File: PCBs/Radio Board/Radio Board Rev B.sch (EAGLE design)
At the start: 10 parts

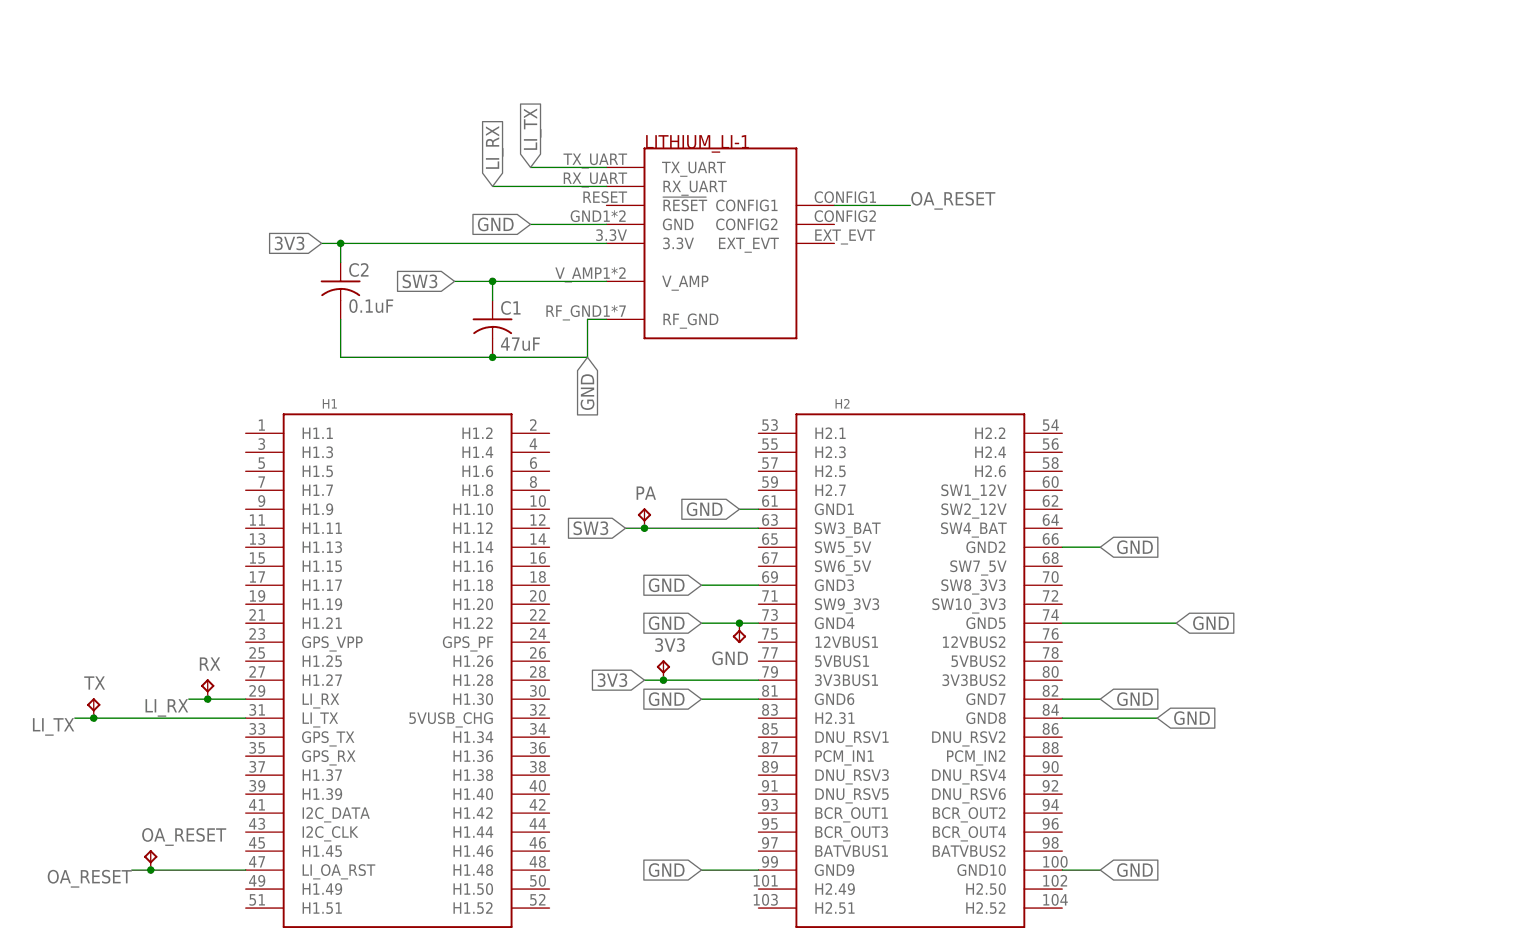
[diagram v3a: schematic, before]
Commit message: Add Molex connector and connector bypass to radio board
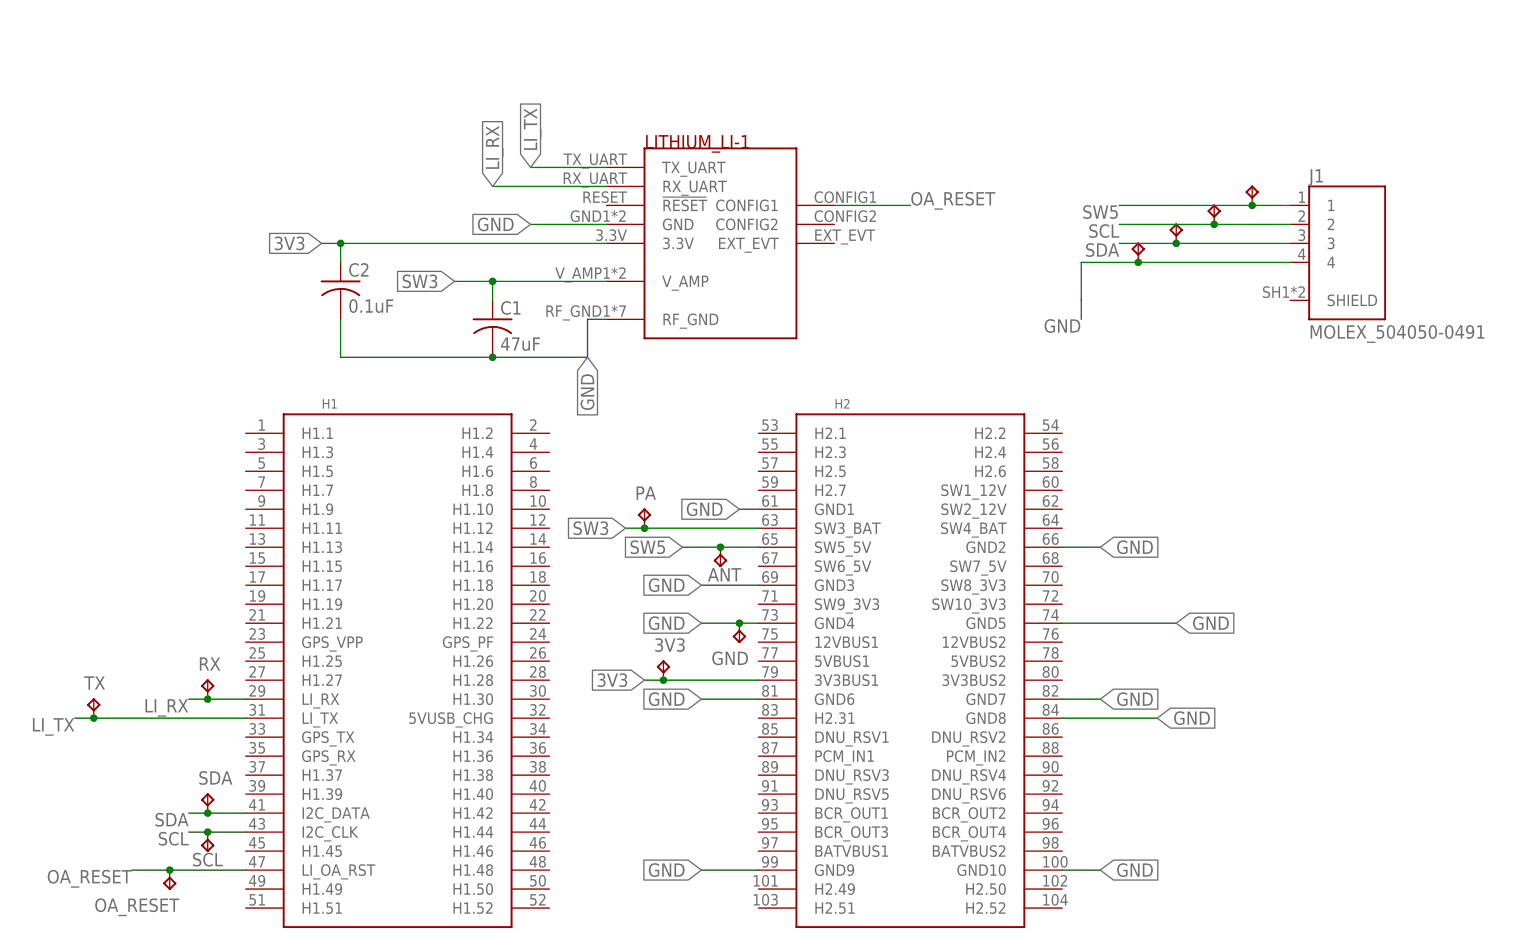
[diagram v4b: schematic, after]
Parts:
- added ANT, J1_1, J1_2, J1_3, J1_4, SCL, SDA: TPTP10SQ, testpad:TPTP10SQ
- added J1: MOLEX_504050-0491, Molex 504050-0491:MOLEX_504050-0491
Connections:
- new net SCL: J1.2, J1_2.TP, SCL.TP, U$1.I2C_CLK
- new net SDA: J1.3, J1_3.TP, SDA.TP, U$1.I2C_DATA
- new net SW5: ANT.TP, J1.1, J1_1.TP, U$1.SW5_5V
- net GND: now also J1.4, J1_4.TP
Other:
- moved on the sheet: OA_RESET
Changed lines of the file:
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@@
 <part name="PA" library="testpad" library_urn="urn:adsk.eagle:library:385" deviceset="TP" device="TP10SQ" package3d_urn="urn:adsk.eagle:package:27962/1"/>
 <part name="GND" library="testpad" library_urn="urn:adsk.eagle:library:385" deviceset="TP" device="TP10SQ" package3d_urn="urn:adsk.eagle:package:27962/1"/>
+<part name="J1" library="Molex 504050-0491" deviceset="MOLEX_504050-0491" device=""/>
+<part name="SDA" library="testpad" library_urn="urn:adsk.eagle:library:385" deviceset="TP" device="TP10SQ" package3d_urn="urn:adsk.eagle:package:27962/1"/>
+<part name="SCL" library="testpad" library_urn="urn:adsk.eagle:library:385" deviceset="TP" device="TP10SQ" package3d_urn="urn:adsk.eagle:package:27962/1"/>
+<part name="ANT" library="testpad" library_urn="urn:adsk.eagle:library:385" deviceset="TP" device="TP10SQ" package3d_urn="urn:adsk.eagle:package:27962/1"/>
+<part name="J1_1" library="testpad" library_urn="urn:adsk.eagle:library:385" deviceset="TP" device="TP10SQ" package3d_urn="urn:adsk.eagle:package:27962/1"/>
+<part name="J1_2" library="testpad" library_urn="urn:adsk.eagle:library:385" deviceset="TP" device="TP10SQ" package3d_urn="urn:adsk.eagle:package:27962/1"/>
+<part name="J1_3" library="testpad" library_urn="urn:adsk.eagle:library:385" deviceset="TP" device="TP10SQ" package3d_urn="urn:adsk.eagle:package:27962/1"/>
+<part name="J1_4" library="testpad" library_urn="urn:adsk.eagle:library:385" deviceset="TP" device="TP10SQ" package3d_urn="urn:adsk.eagle:package:27962/1"/>
 </parts>
 <sheets>
@@
 <instance part="RX" gate="G$1" x="17.78" y="33.02"/>
 <instance part="TX" gate="G$1" x="2.54" y="30.48"/>
-<instance part="OA_RESET" gate="G$1" x="10.16" y="10.16"/>
+<instance part="OA_RESET" gate="G$1" x="12.7" y="5.08" rot="R180"/>
 <instance part="PA" gate="G$1" x="76.2" y="55.88"/>
 <instance part="GND" gate="G$1" x="88.9" y="38.1" rot="R180"/>
+<instance part="J1" gate="G$1" x="170.18" y="91.44"/>
+<instance part="SDA" gate="G$1" x="17.78" y="17.78"/>
+<instance part="SCL" gate="G$1" x="17.78" y="10.16" smashed="yes" rot="R180">
+<attribute name="NAME" x="19.812" y="9.906" size="1.778" layer="95" rot="R180"/>
+<attribute name="TP_SIGNAL_NAME" x="16.51" y="11.43" size="1.778" layer="97" rot="R180"/>
+</instance>
+<instance part="ANT" gate="G$1" x="86.36" y="48.26" smashed="yes" rot="R180">
+<attribute name="NAME" x="89.154" y="48.006" size="1.778" layer="95" rot="R180"/>
+<attribute name="TP_SIGNAL_NAME" x="85.09" y="49.53" size="1.778" layer="97" rot="R180"/>
+</instance>
+<instance part="J1_1" gate="G$1" x="157.48" y="99.06" smashed="yes">
+<attribute name="TP_SIGNAL_NAME" x="158.75" y="97.79" size="1.778" layer="97"/>
+</instance>
+<instance part="J1_2" gate="G$1" x="152.4" y="96.52" smashed="yes">
+<attribute name="TP_SIGNAL_NAME" x="153.67" y="95.25" size="1.778" layer="97"/>
+</instance>
+<instance part="J1_3" gate="G$1" x="147.32" y="93.98" smashed="yes">
+<attribute name="TP_SIGNAL_NAME" x="148.59" y="92.71" size="1.778" layer="97"/>
+</instance>
+<instance part="J1_4" gate="G$1" x="142.24" y="91.44" smashed="yes">
+<attribute name="TP_SIGNAL_NAME" x="143.51" y="90.17" size="1.778" layer="97"/>
+</instance>
 </instances>
 <busses>
@@
 <pinref part="LI-1" gate="G$1" pin="RF_GND"/>
 </segment>
+<segment>
+<wire x1="134.62" y1="83.82" x2="134.62" y2="81.28" width="0.1524" layer="91"/>
+<label x="134.62" y="81.28" size="1.778" layer="95" rot="R180"/>
+<pinref part="J1" gate="G$1" pin="4"/>
+<wire x1="162.56" y1="88.9" x2="142.24" y2="88.9" width="0.1524" layer="91"/>
+<wire x1="142.24" y1="88.9" x2="134.62" y2="88.9" width="0.1524" layer="91"/>
+<wire x1="134.62" y1="88.9" x2="134.62" y2="83.82" width="0.1524" layer="91"/>
+<pinref part="J1_4" gate="G$1" pin="TP"/>
+<junction x="142.24" y="88.9"/>
+</segment>
 </net>
 <net name="SW3" class="0">
@@
 </segment>
 <segment>
-<wire x1="22.86" y1="7.62" x2="10.16" y2="7.62" width="0.1524" layer="91"/>
+<wire x1="22.86" y1="7.62" x2="12.7" y2="7.62" width="0.1524" layer="91"/>
 <label x="7.62" y="7.62" size="1.778" layer="95" rot="R180"/>
 <pinref part="U$1" gate="A" pin="LI_OA_RST"/>
 <pinref part="OA_RESET" gate="G$1" pin="TP"/>
-<wire x1="10.16" y1="7.62" x2="7.62" y2="7.62" width="0.1524" layer="91"/>
-<junction x="10.16" y="7.62"/>
+<wire x1="12.7" y1="7.62" x2="7.62" y2="7.62" width="0.1524" layer="91"/>
+<junction x="12.7" y="7.62"/>
 </segment>
 </net>
@@
 </segment>
 </net>
+<net name="SW5" class="0">
+<segment>
+<pinref part="J1" gate="G$1" pin="1"/>
+<wire x1="162.56" y1="96.52" x2="157.48" y2="96.52" width="0.1524" layer="91"/>
+<label x="139.7" y="96.52" size="1.778" layer="95" rot="R180"/>
+<pinref part="J1_1" gate="G$1" pin="TP"/>
+<wire x1="157.48" y1="96.52" x2="139.7" y2="96.52" width="0.1524" layer="91"/>
+<junction x="157.48" y="96.52"/>
+</segment>
+<segment>
+<pinref part="U$1" gate="A" pin="SW5_5V"/>
+<wire x1="91.44" y1="50.8" x2="86.36" y2="50.8" width="0.1524" layer="91"/>
+<label x="81.28" y="50.8" size="1.778" layer="95" rot="R180" xref="yes"/>
+<pinref part="ANT" gate="G$1" pin="TP"/>
+<wire x1="86.36" y1="50.8" x2="81.28" y2="50.8" width="0.1524" layer="91"/>
+<junction x="86.36" y="50.8"/>
+</segment>
+</net>
+<net name="SCL" class="0">
+<segment>
+<pinref part="J1" gate="G$1" pin="2"/>
+<wire x1="162.56" y1="93.98" x2="152.4" y2="93.98" width="0.1524" layer="91"/>
+<label x="139.7" y="93.98" size="1.778" layer="95" rot="R180"/>
+<pinref part="J1_2" gate="G$1" pin="TP"/>
+<wire x1="152.4" y1="93.98" x2="139.7" y2="93.98" width="0.1524" layer="91"/>
+<junction x="152.4" y="93.98"/>
+</segment>
+<segment>
+<pinref part="U$1" gate="A" pin="I2C_CLK"/>
+<wire x1="22.86" y1="12.7" x2="17.78" y2="12.7" width="0.1524" layer="91"/>
+<label x="15.24" y="12.7" size="1.778" layer="95" rot="R180"/>
+<pinref part="SCL" gate="G$1" pin="TP"/>
+<wire x1="17.78" y1="12.7" x2="15.24" y2="12.7" width="0.1524" layer="91"/>
+<junction x="17.78" y="12.7"/>
+</segment>
+</net>
+<net name="SDA" class="0">
+<segment>
+<pinref part="J1" gate="G$1" pin="3"/>
+<wire x1="162.56" y1="91.44" x2="147.32" y2="91.44" width="0.1524" layer="91"/>
+<label x="139.7" y="91.44" size="1.778" layer="95" rot="R180"/>
+<pinref part="J1_3" gate="G$1" pin="TP"/>
+<wire x1="147.32" y1="91.44" x2="139.7" y2="91.44" width="0.1524" layer="91"/>
+<junction x="147.32" y="91.44"/>
+</segment>
+<segment>
+<pinref part="U$1" gate="A" pin="I2C_DATA"/>
+<wire x1="22.86" y1="15.24" x2="17.78" y2="15.24" width="0.1524" layer="91"/>
+<label x="15.24" y="15.24" size="1.778" layer="95" rot="R180"/>
+<pinref part="SDA" gate="G$1" pin="TP"/>
+<wire x1="17.78" y1="15.24" x2="15.24" y2="15.24" width="0.1524" layer="91"/>
+<junction x="17.78" y="15.24"/>
+</segment>
+</net>

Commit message: Move MicroLock connector
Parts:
- removed J1_1, J1_2, J1_3, J1_4: TPTP10SQ, testpad:TPTP10SQ
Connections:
- net GND: no longer J1_4.TP
- net SCL: no longer J1_2.TP
- net SDA: no longer J1_3.TP
- net SW5: no longer J1_1.TP
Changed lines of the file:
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@@
 <part name="SCL" library="testpad" library_urn="urn:adsk.eagle:library:385" deviceset="TP" device="TP10SQ" package3d_urn="urn:adsk.eagle:package:27962/1"/>
 <part name="ANT" library="testpad" library_urn="urn:adsk.eagle:library:385" deviceset="TP" device="TP10SQ" package3d_urn="urn:adsk.eagle:package:27962/1"/>
-<part name="J1_1" library="testpad" library_urn="urn:adsk.eagle:library:385" deviceset="TP" device="TP10SQ" package3d_urn="urn:adsk.eagle:package:27962/1"/>
-<part name="J1_2" library="testpad" library_urn="urn:adsk.eagle:library:385" deviceset="TP" device="TP10SQ" package3d_urn="urn:adsk.eagle:package:27962/1"/>
-<part name="J1_3" library="testpad" library_urn="urn:adsk.eagle:library:385" deviceset="TP" device="TP10SQ" package3d_urn="urn:adsk.eagle:package:27962/1"/>
-<part name="J1_4" library="testpad" library_urn="urn:adsk.eagle:library:385" deviceset="TP" device="TP10SQ" package3d_urn="urn:adsk.eagle:package:27962/1"/>
 </parts>
 <sheets>
@@
 <attribute name="TP_SIGNAL_NAME" x="85.09" y="49.53" size="1.778" layer="97" rot="R180"/>
 </instance>
-<instance part="J1_1" gate="G$1" x="157.48" y="99.06" smashed="yes">
-<attribute name="TP_SIGNAL_NAME" x="158.75" y="97.79" size="1.778" layer="97"/>
-</instance>
-<instance part="J1_2" gate="G$1" x="152.4" y="96.52" smashed="yes">
-<attribute name="TP_SIGNAL_NAME" x="153.67" y="95.25" size="1.778" layer="97"/>
-</instance>
-<instance part="J1_3" gate="G$1" x="147.32" y="93.98" smashed="yes">
-<attribute name="TP_SIGNAL_NAME" x="148.59" y="92.71" size="1.778" layer="97"/>
-</instance>
-<instance part="J1_4" gate="G$1" x="142.24" y="91.44" smashed="yes">
-<attribute name="TP_SIGNAL_NAME" x="143.51" y="90.17" size="1.778" layer="97"/>
-</instance>
 </instances>
 <busses>
@@
 <wire x1="142.24" y1="88.9" x2="134.62" y2="88.9" width="0.1524" layer="91"/>
 <wire x1="134.62" y1="88.9" x2="134.62" y2="83.82" width="0.1524" layer="91"/>
-<pinref part="J1_4" gate="G$1" pin="TP"/>
-<junction x="142.24" y="88.9"/>
 </segment>
 </net>
@@
 <wire x1="162.56" y1="96.52" x2="157.48" y2="96.52" width="0.1524" layer="91"/>
 <label x="139.7" y="96.52" size="1.778" layer="95" rot="R180"/>
-<pinref part="J1_1" gate="G$1" pin="TP"/>
 <wire x1="157.48" y1="96.52" x2="139.7" y2="96.52" width="0.1524" layer="91"/>
-<junction x="157.48" y="96.52"/>
 </segment>
 <segment>
@@
 <wire x1="162.56" y1="93.98" x2="152.4" y2="93.98" width="0.1524" layer="91"/>
 <label x="139.7" y="93.98" size="1.778" layer="95" rot="R180"/>
-<pinref part="J1_2" gate="G$1" pin="TP"/>
 <wire x1="152.4" y1="93.98" x2="139.7" y2="93.98" width="0.1524" layer="91"/>
-<junction x="152.4" y="93.98"/>
 </segment>
 <segment>
@@
 <wire x1="162.56" y1="91.44" x2="147.32" y2="91.44" width="0.1524" layer="91"/>
 <label x="139.7" y="91.44" size="1.778" layer="95" rot="R180"/>
-<pinref part="J1_3" gate="G$1" pin="TP"/>
 <wire x1="147.32" y1="91.44" x2="139.7" y2="91.44" width="0.1524" layer="91"/>
-<junction x="147.32" y="91.44"/>
-</segment>
-<segment>
+</segment>
+<segment>

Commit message: Split I2C and SPI buses
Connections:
- removed net SCL: J1.2, SCL.TP, U$1.I2C_CLK
- removed net SDA: J1.3, SDA.TP, U$1.I2C_DATA
- new net SCL_ANT: J1.2, SCL.TP, U$1.SCL_ANT
- new net SDA_ANT: J1.3, SDA.TP, U$1.SDA_ANT
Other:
- moved on the sheet: SCL, SDA
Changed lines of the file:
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@@
 <instance part="GND" gate="G$1" x="88.9" y="38.1" rot="R180"/>
 <instance part="J1" gate="G$1" x="170.18" y="91.44"/>
-<instance part="SDA" gate="G$1" x="17.78" y="17.78"/>
-<instance part="SCL" gate="G$1" x="17.78" y="10.16" smashed="yes" rot="R180">
-<attribute name="NAME" x="19.812" y="9.906" size="1.778" layer="95" rot="R180"/>
-<attribute name="TP_SIGNAL_NAME" x="16.51" y="11.43" size="1.778" layer="97" rot="R180"/>
+<instance part="SDA" gate="G$1" x="15.24" y="22.86"/>
+<instance part="SCL" gate="G$1" x="15.24" y="15.24" smashed="yes" rot="R180">
+<attribute name="NAME" x="17.272" y="14.986" size="1.778" layer="95" rot="R180"/>
+<attribute name="TP_SIGNAL_NAME" x="13.97" y="16.51" size="1.778" layer="97" rot="R180"/>
 </instance>
 <instance part="ANT" gate="G$1" x="86.36" y="48.26" smashed="yes" rot="R180">
@@
 </segment>
 </net>
-<net name="SCL" class="0">
+<net name="SCL_ANT" class="0">
 <segment>
 <pinref part="J1" gate="G$1" pin="2"/>
@@
 </segment>
 <segment>
-<pinref part="U$1" gate="A" pin="I2C_CLK"/>
-<wire x1="22.86" y1="12.7" x2="17.78" y2="12.7" width="0.1524" layer="91"/>
-<label x="15.24" y="12.7" size="1.778" layer="95" rot="R180"/>
+<label x="12.7" y="17.78" size="1.778" layer="95" rot="R180"/>
 <pinref part="SCL" gate="G$1" pin="TP"/>
-<wire x1="17.78" y1="12.7" x2="15.24" y2="12.7" width="0.1524" layer="91"/>
-<junction x="17.78" y="12.7"/>
-</segment>
-</net>
-<net name="SDA" class="0">
+<wire x1="15.24" y1="17.78" x2="12.7" y2="17.78" width="0.1524" layer="91"/>
+<pinref part="U$1" gate="A" pin="SCL_ANT"/>
+<wire x1="15.24" y1="17.78" x2="22.86" y2="17.78" width="0.1524" layer="91"/>
+<junction x="15.24" y="17.78"/>
+</segment>
+</net>
+<net name="SDA_ANT" class="0">
 <segment>
 <pinref part="J1" gate="G$1" pin="3"/>
@@
 </segment>
 <segment>
-<pinref part="U$1" gate="A" pin="I2C_DATA"/>
-<wire x1="22.86" y1="15.24" x2="17.78" y2="15.24" width="0.1524" layer="91"/>
-<label x="15.24" y="15.24" size="1.778" layer="95" rot="R180"/>
+<label x="12.7" y="20.32" size="1.778" layer="95" rot="R180"/>
 <pinref part="SDA" gate="G$1" pin="TP"/>
-<wire x1="17.78" y1="15.24" x2="15.24" y2="15.24" width="0.1524" layer="91"/>
-<junction x="17.78" y="15.24"/>
-</segment>
-</net>
+<wire x1="15.24" y1="20.32" x2="12.7" y2="20.32" width="0.1524" layer="91"/>
+<pinref part="U$1" gate="A" pin="SDA_ANT"/>
+<wire x1="15.24" y1="20.32" x2="22.86" y2="20.32" width="0.1524" layer="91"/>
+<junction x="15.24" y="20.32"/>
+</segment>
+</net>
